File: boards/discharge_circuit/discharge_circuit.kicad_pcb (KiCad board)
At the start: 2 copper layers, 13 parts, among them J1 Unfused TS, J2 Shutdown Circuit, J3 TSMP, J4 TSAL, J5 IMD, J6 EM/Precharge, K1 G2RL-1-E

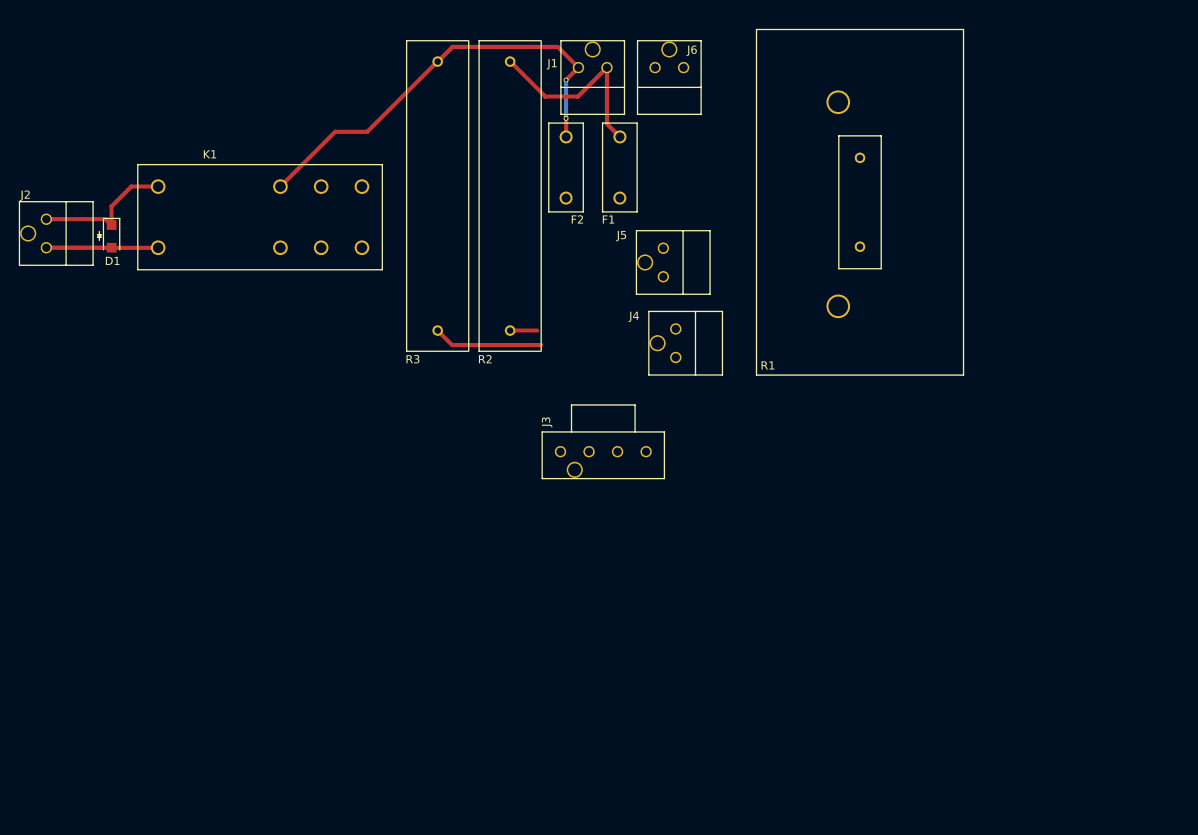
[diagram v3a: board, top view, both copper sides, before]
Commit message: added layout and tracing for the discharge board
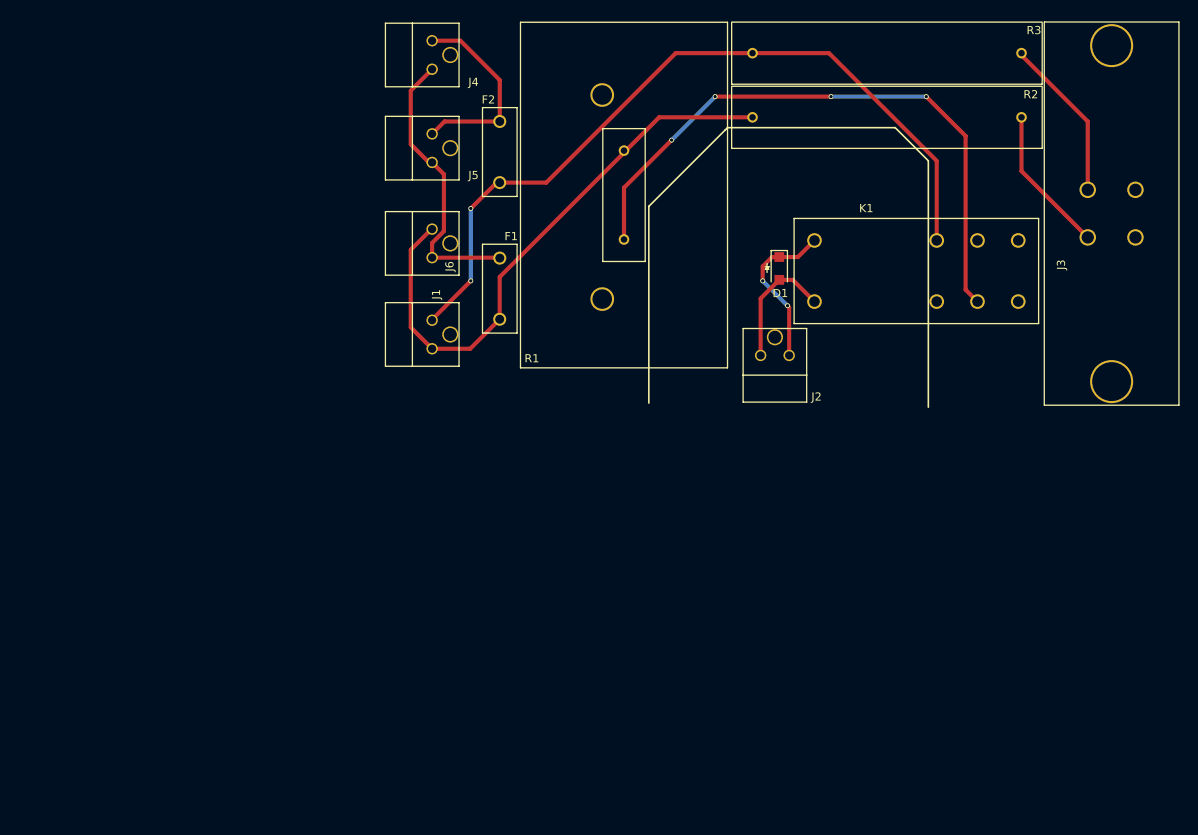
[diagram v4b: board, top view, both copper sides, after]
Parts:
- J3: footprint footprints:Ultrafit_4 -> footprints:mx150l_2
- moved J2 88.6 mm to (146.3, 70.4), turned to 90 degrees
- moved D1 82.0 mm to (148.6, 59.7)
- moved K1 80.8 mm to (152.9, 63.8)
- moved R3 79.3 mm to (178.3, 33.3), turned to 180 degrees
- moved R2 68.0 mm to (178.3, 41.1), turned to 180 degrees
- moved J3 65.0 mm to (186.4, 55.9), turned to 90 degrees
- moved J4 49.0 mm to (106.0, 31.8), turned to 0 degrees
- moved J1 35.8 mm to (106.0, 66.0), turned to 0 degrees
- moved J6 33.8 mm to (106.0, 54.9), turned to 0 degrees
- moved J5 33.3 mm to (106.0, 43.2), turned to 0 degrees
- moved R1 29.0 mm to (129.5, 56.1)
- moved F1 16.5 mm to (114.3, 58.4), turned to 270 degrees
- moved F2 12.4 mm to (114.3, 41.7), turned to 270 degrees
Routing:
- net Net-(K1-Pad6): track 0.00 -> 75.8 mm, vias 0 -> 4
- net /TS+Unfused: track 24.3 -> 70.9 mm
- net /TS-Unfused: track 53.9 -> 96.0 mm
- net /TS+Fused: track 0.00 -> 35.1 mm
- net /TS-Fused: track 0.00 -> 24.3 mm
- net Net-(J3-Pad1): track 3.30 -> 18.1 mm
- net Net-(J3-Pad2): track 13.4 -> 20.1 mm
- net /Shutdown: track 17.3 -> 19.9 mm, vias 0 -> 2
- net GND: track 13.7 -> 15.6 mm
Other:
- rule via_min_drill: 0.3 -> 0.3048

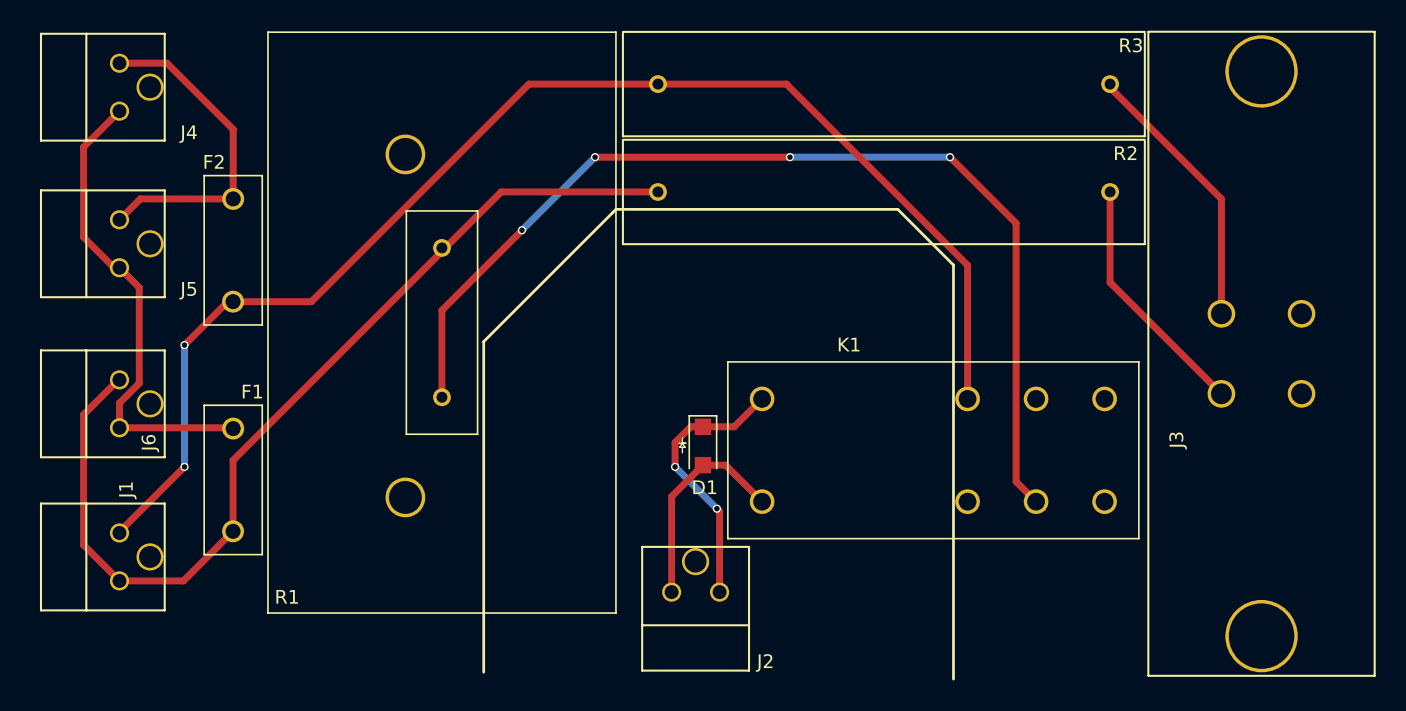
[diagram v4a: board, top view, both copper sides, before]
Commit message: added revisions to discharge circuit
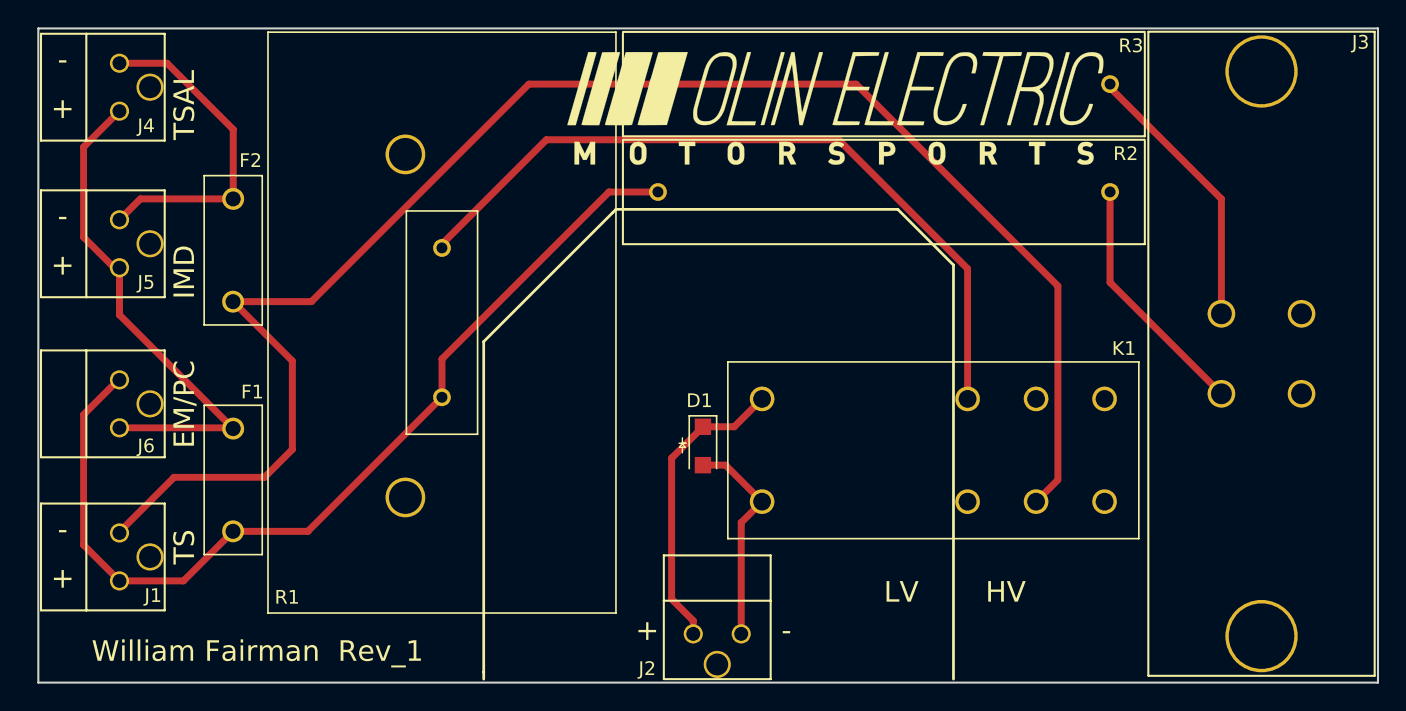
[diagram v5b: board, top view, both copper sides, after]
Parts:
- added G***: LOGO, footprints:Logo_Large, F.Cu at (158.2, 35.1)
- moved J2 5.92 mm to (151.4, 73.4), turned to 270 degrees
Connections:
- K1 pad 2: /TS-Unfused -> Net-(K1-Pad2)
- K1 pad 6: Net-(K1-Pad6) -> /TS-Unfused
- R1 pad 1: Net-(K1-Pad6) -> /TS+Unfused
- R1 pad 2: /TS+Unfused -> Net-(K1-Pad2)
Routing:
- net Net-(K1-Pad6): track 75.8 -> 0.00 mm, vias 4 -> 0
- net Net-(K1-Pad2): track 0.00 -> 55.4 mm
- net /TS-Unfused: track 96.0 -> 117.4 mm, vias 2 -> 0
- net /TS+Fused: track 35.1 -> 37.4 mm
- net /Shutdown: track 19.9 -> 21.9 mm, vias 2 -> 0
- net /TS+Unfused: track 70.9 -> 69.6 mm
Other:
- board outline added: 97.8 x 47.8 mm
- board text added: "+"
- board text added: "-"
- board text added: "EM/PC"
- board text added: "HV"
- board text added: "IMD"
- board text added: "LV"
- board text added: "TS"
- board text added: "TSAL"
- board text added: "William Fairman Rev_1"

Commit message: one more revision
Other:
- board text added: "F"
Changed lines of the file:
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@@
     (links 19)
     (no_connects 0)
-    (area 100.000999 29.134999 197.941001 77.037001)
+    (area 89.126288 22.954 197.941001 78.9038)
     (thickness 1.6)
-    (drawings 30)
+    (drawings 31)
     (tracks 60)
     (zones 0)
@@
       (xy 18.232145 -4.0226) (xy 18.481106 -4.090329) (xy 18.746513 -4.111367) (xy 18.846075 -4.107132)) (layer F.SilkS) (width 0.01))
   )
+  (gr_text F (at 101.854 58.42) (layer F.SilkS)
+    (effects (font (size 1.5 1.5) (thickness 0.3)))
+  )
   (gr_text "William Fairman  Rev_1" (at 116.078 74.676) (layer F.SilkS)

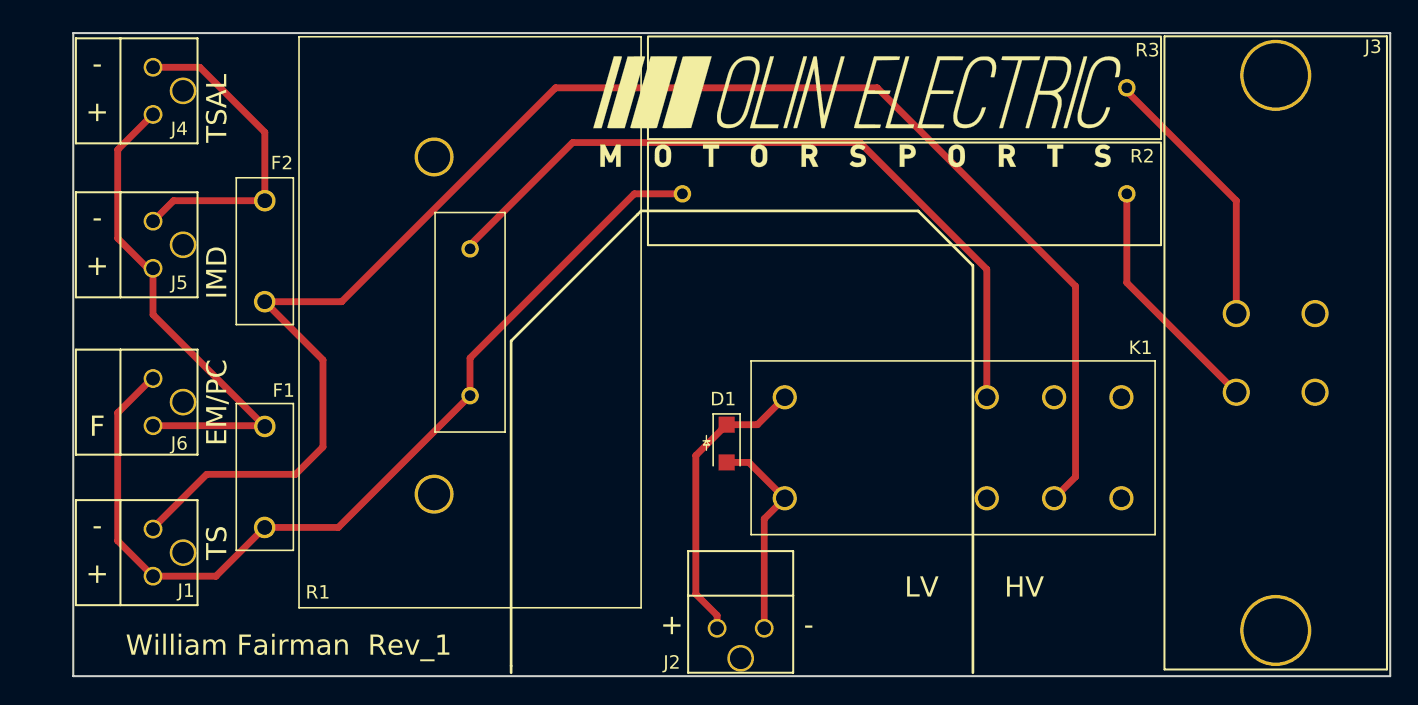
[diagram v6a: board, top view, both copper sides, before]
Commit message: added gerber files to discharge circuit
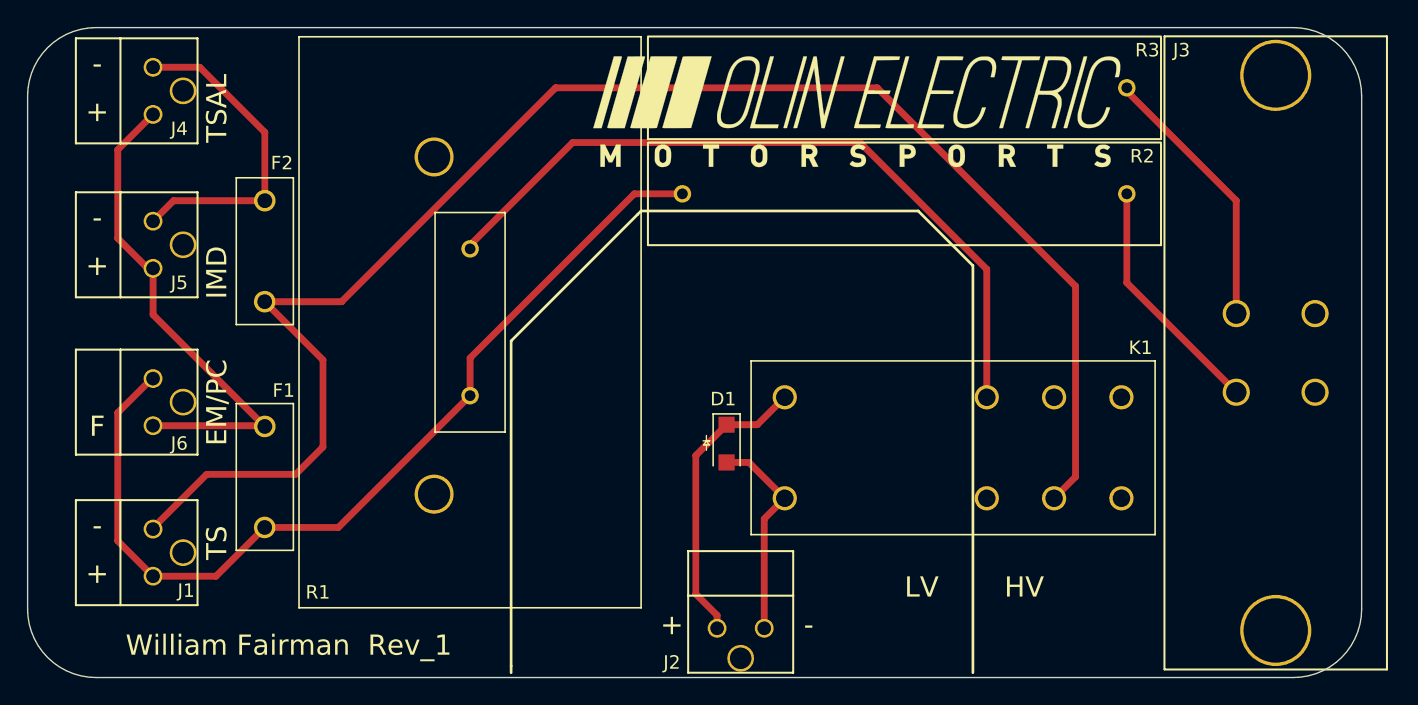
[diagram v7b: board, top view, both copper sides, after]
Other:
- board size 97.8 x 47.8 mm -> 99.1 x 48.3 mm
- rule via_min_size: 0.4 -> 0.381
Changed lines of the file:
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@@
     (links 19)
     (no_connects 0)
-    (area 89.126288 22.954 197.941001 78.9038)
+    (area 96.635099 27.3682 197.750501 78.9038)
     (thickness 1.6)
-    (drawings 31)
+    (drawings 33)
     (tracks 60)
     (zones 0)
@@
     (via_size 0.6)
     (via_drill 0.4)
-    (via_min_size 0.4)
+    (via_min_size 0.381)
     (via_min_drill 0.3048)
     (uvia_size 0.3)
@@
     (visible_elements FFFFFF7F)
     (pcbplotparams
-      (layerselection 0x00030_80000001)
+      (layerselection 0x010f0_80000001)
       (usegerberextensions false)
       (excludeedgelayer true)
@@
       (outputformat 1)
       (mirror false)
-      (drillshape 1)
+      (drillshape 0)
       (scaleselection 1)
       (outputdirectory ""))
@@
   (module footprints:mx150l_2 (layer F.Cu)
     (at 186.436 55.88 90)
-    (fp_text reference J3 (at 25.654 10.16 180) (layer F.SilkS)
+    (fp_text reference J3 (at 25.4 -4.064 180) (layer F.SilkS)
       (effects (font (size 1 1) (thickness 0.15)))
     )
@@
       (xy 18.232145 -4.0226) (xy 18.481106 -4.090329) (xy 18.746513 -4.111367) (xy 18.846075 -4.107132)) (layer F.SilkS) (width 0.01))
   )
+  (gr_line (start 195.7451 33.8836) (end 195.7451 71.9836) (layer Edge.Cuts) (width 0.1))
+  (gr_line (start 101.7651 77.0636) (end 190.6651 77.0636) (layer Edge.Cuts) (width 0.1))
+  (gr_line (start 96.6851 33.8836) (end 96.6851 71.9836) (layer Edge.Cuts) (width 0.1))
+  (gr_line (start 101.7651 28.8036) (end 190.6651 28.8036) (layer Edge.Cuts) (width 0.1))
+  (gr_arc (start 101.7651 33.8836) (end 101.7651 28.8036) (angle -90) (layer Edge.Cuts) (width 0.1))
+  (gr_arc (start 101.7651 71.9836) (end 96.6851 71.9836) (angle -90) (layer Edge.Cuts) (width 0.1))
+  (gr_arc (start 190.6651 71.9836) (end 190.6651 77.0636) (angle -90) (layer Edge.Cuts) (width 0.1))
+  (gr_arc (start 190.6651 33.8836) (end 195.7451 33.8836) (angle -90) (layer Edge.Cuts) (width 0.1))
   (gr_text F (at 101.854 58.42) (layer F.SilkS)
     (effects (font (size 1.5 1.5) (thickness 0.3)))
@@
     (effects (font (size 1.5 1.5) (thickness 0.3)))
   )
-  (dimension 47.752 (width 0.3) (layer F.SilkS)
-    (gr_text "1.8800 in" (at 94.662001 53.086 270) (layer F.SilkS)
-      (effects (font (size 1.5 1.5) (thickness 0.3)))
-    )
-    (feature1 (pts (xy 99.06 76.962) (xy 93.312001 76.962)))
-    (feature2 (pts (xy 99.06 29.21) (xy 93.312001 29.21)))
-    (crossbar (pts (xy 96.012001 29.21) (xy 96.012001 76.962)))
-    (arrow1a (pts (xy 96.012001 76.962) (xy 95.42558 75.835496)))
-    (arrow1b (pts (xy 96.012001 76.962) (xy 96.598422 75.835496)))
-    (arrow2a (pts (xy 96.012001 29.21) (xy 95.42558 30.336504)))
-    (arrow2b (pts (xy 96.012001 29.21) (xy 96.598422 30.336504)))
-  )
-  (dimension 97.79 (width 0.3) (layer F.SilkS)
-    (gr_text "3.8500 in" (at 148.971 24.304) (layer F.SilkS)
-      (effects (font (size 1.5 1.5) (thickness 0.3)))
-    )
-    (feature1 (pts (xy 197.866 28.448) (xy 197.866 22.954)))
-    (feature2 (pts (xy 100.076 28.448) (xy 100.076 22.954)))
-    (crossbar (pts (xy 100.076 25.654) (xy 197.866 25.654)))
-    (arrow1a (pts (xy 197.866 25.654) (xy 196.739496 26.240421)))
-    (arrow1b (pts (xy 197.866 25.654) (xy 196.739496 25.067579)))
-    (arrow2a (pts (xy 100.076 25.654) (xy 101.202504 26.240421)))
-    (arrow2b (pts (xy 100.076 25.654) (xy 101.202504 25.067579)))
-  )
   (gr_line (start 132.588 76.2) (end 132.588 76.708) (angle 90) (layer F.SilkS) (width 0.2))
-  (gr_line (start 197.866 29.21) (end 197.866 76.962) (angle 90) (layer Edge.Cuts) (width 0.15))
-  (gr_line (start 100.076 29.21) (end 197.866 29.21) (angle 90) (layer Edge.Cuts) (width 0.15))
-  (gr_line (start 100.076 76.962) (end 100.076 29.21) (angle 90) (layer Edge.Cuts) (width 0.15))
-  (gr_line (start 197.866 76.962) (end 100.076 76.962) (angle 90) (layer Edge.Cuts) (width 0.15))
   (dimension 12.954 (width 0.3) (layer F.SilkS)
     (gr_text "0.5100 in" (at 160.401 49.196) (layer F.SilkS)
